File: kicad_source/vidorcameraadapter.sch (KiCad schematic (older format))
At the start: 9 parts, among them CN1 CONN_02X26, CN2 CONN_02X10, CN3 CONN_01X03

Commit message: corrected spacers, added resistors, made layout
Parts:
- added R1, R10, R11, R12, R13, R14, R15, R16, R17, R18, R2, R3, R4, R5, R6, R7, R8, R9: R_0603, resistors:R_0603, symbol devices:R_0603
- MECH1, MECH2: value WA-SMSI_9774010243 -> WA-SMSI_9774015151; footprint MECH_smd-spacer:WA-SMSI_9774010243 -> MECH_smd-spacer:WA-SMSI_9774015151; symbol MECH_smd-spacer:WA-SMSI_9774010243 -> MECH_smd-spacer:WA-SMSI_9774015151
- MECH3, MECH4, MECH5, MECH6: value WA-SMSI_9774010243 -> WA-SMSI_97730606334; footprint MECH_smd-spacer:WA-SMSI_9774010243 -> MECH_smd-spacer:WA-SMSI_97730606334; symbol MECH_smd-spacer:WA-SMSI_9774010243 -> MECH_smd-spacer:WA-SMSI_97730606334
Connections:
- net labels added: DOUT0_R, DOUT1_R, DOUT2_R, DOUT3_R, DOUT4_R, DOUT5_R, DOUT6_R, DOUT7_R, DOUT8_R, DOUT9_R, HREF_R, PCLK_R, PWDN_R, RST_R, SCL_R, SDA_R, VSYNC_R, XCLK_R
- wire segments 97 -> 115
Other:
- moved on the sheet: CN2

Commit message: added 3d models, added mounting holes
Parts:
- CN2: footprint pin_headers:Pin_Header_Straight_2x10 -> CON_wuerth:WR-PHD_61302021821
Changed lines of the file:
@@
 F 0 "CN2" H 7200 2665 50  0000 C CNN
 F 1 "CONN_02X10" H 7200 2574 50  0000 C CNN
-F 2 "pin_headers:Pin_Header_Straight_2x10" H 7200 2573 50  0001 C CNN
+F 2 "CON_wuerth:WR-PHD_61302021821" H 7200 2573 50  0001 C CNN
 F 3 "" H 7200 800 50  0000 C CNN
 	1    7200 2000

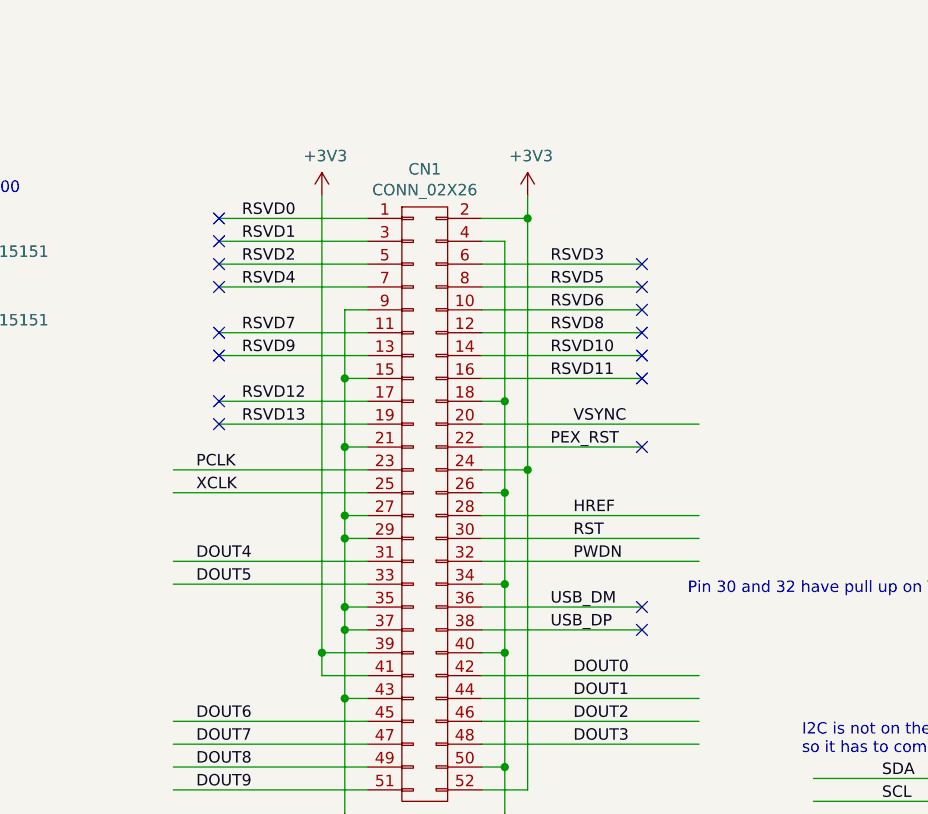
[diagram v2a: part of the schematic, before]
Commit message: added testpoints for all unused pins
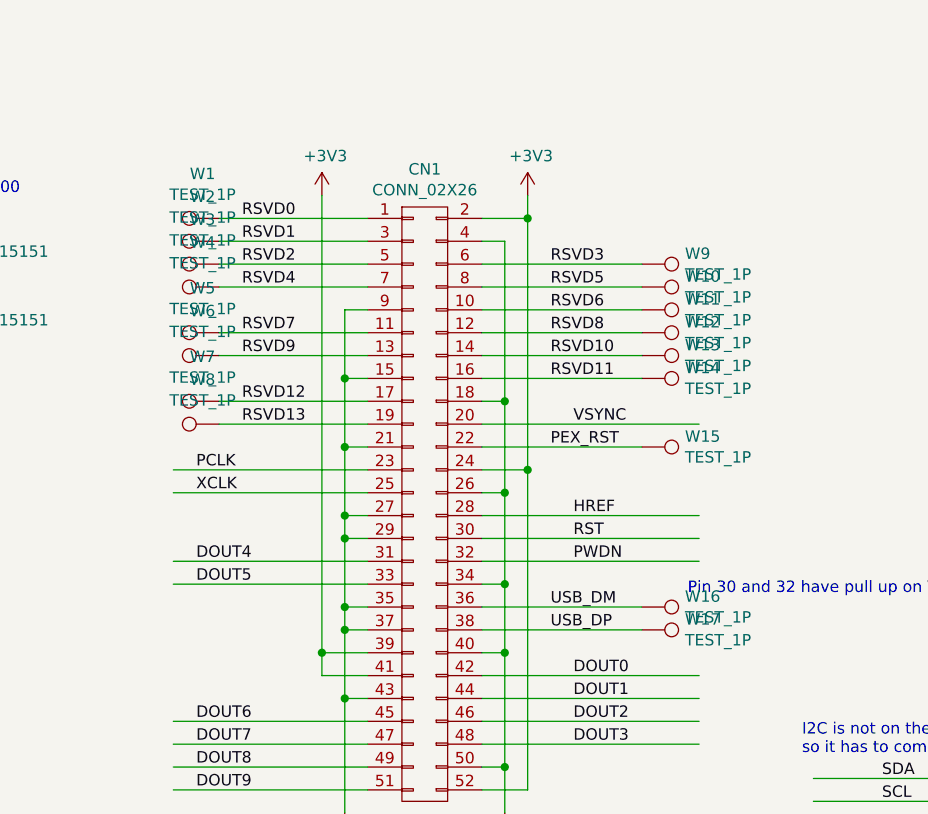
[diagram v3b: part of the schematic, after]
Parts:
- added W1, W10, W11, W12, W13, W14, W15, W16, W17, W2, W3, W4, W5, W6, W7, W8, W9: TEST_1P, wire_pads:SolderWirePad_single_1mmSMD, symbol mechanical-connectors:TEST_1P
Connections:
- no-connect marks 23 -> 6
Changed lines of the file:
@@
 Text Label 4100 6000 0    50   ~ 0
 USB_DP
-NoConn ~ 4500 5900
-NoConn ~ 4500 6000
 $Comp
 L mechanical-connectors:CONN_02X10 CN2
@@
 Text Notes 4700 5850 0    50   ~ 0
 Pin 30 and 32 have pull up on Vidor 4000
-NoConn ~ 4500 5200
 Wire Wire Line
 	2650 4200 3300 4200
@@
 Text Label 2750 5100 0    50   ~ 0
 RSVD13
-NoConn ~ 4500 4400
-NoConn ~ 4500 4500
-NoConn ~ 4500 4600
-NoConn ~ 4500 4700
-NoConn ~ 4500 4800
-NoConn ~ 4500 4900
-NoConn ~ 2650 4200
-NoConn ~ 2650 4300
-NoConn ~ 2650 4400
-NoConn ~ 2650 4500
-NoConn ~ 2650 4700
-NoConn ~ 2650 4800
-NoConn ~ 2650 5000
-NoConn ~ 2650 5100
 $Comp
 L MECH_smd-spacer:WA-SMSI_9774015151 MECH1
@@
 Text Label 7750 2050 0    50   ~ 0
 DOUT6_R
+$Comp
+L mechanical-connectors:TEST_1P W9
+U 1 1 5E310C83
+P 4500 4400
+F 0 "W9" V 4454 4588 50  0000 L CNN
+F 1 "TEST_1P" V 4545 4588 50  0000 L CNN
+F 2 "wire_pads:SolderWirePad_single_1mmSMD" V 4591 4588 50  0001 L CNN
+F 3 "" H 4700 4400 50  0000 C CNN
+	1    4500 4400
+	0    1    1    0
+$EndComp
+$Comp
+L mechanical-connectors:TEST_1P W10
+U 1 1 5E3153CE
+P 4500 4500
+F 0 "W10" V 4454 4688 50  0000 L CNN
+F 1 "TEST_1P" V 4545 4688 50  0000 L CNN
+F 2 "wire_pads:SolderWirePad_single_1mmSMD" V 4591 4688 50  0001 L CNN
+F 3 "" H 4700 4500 50  0000 C CNN
+	1    4500 4500
+	0    1    1    0
+$EndComp
+$Comp
+L mechanical-connectors:TEST_1P W11
+U 1 1 5E31571A
+P 4500 4600
+F 0 "W11" V 4454 4788 50  0000 L CNN
+F 1 "TEST_1P" V 4545 4788 50  0000 L CNN
+F 2 "wire_pads:SolderWirePad_single_1mmSMD" V 4591 4788 50  0001 L CNN
+F 3 "" H 4700 4600 50  0000 C CNN
+	1    4500 4600
+	0    1    1    0
+$EndComp
+$Comp
+L mechanical-connectors:TEST_1P W12
+U 1 1 5E3158F5
+P 4500 4700
+F 0 "W12" V 4454 4888 50  0000 L CNN
+F 1 "TEST_1P" V 4545 4888 50  0000 L CNN
+F 2 "wire_pads:SolderWirePad_single_1mmSMD" V 4591 4888 50  0001 L CNN
+F 3 "" H 4700 4700 50  0000 C CNN
+	1    4500 4700
+	0    1    1    0
+$EndComp
+$Comp
+L mechanical-connectors:TEST_1P W13
+U 1 1 5E315B8E
+P 4500 4800
+F 0 "W13" V 4454 4988 50  0000 L CNN
+F 1 "TEST_1P" V 4545 4988 50  0000 L CNN
+F 2 "wire_pads:SolderWirePad_single_1mmSMD" V 4591 4988 50  0001 L CNN
+F 3 "" H 4700 4800 50  0000 C CNN
+	1    4500 4800
+	0    1    1    0
+$EndComp
+$Comp
+L mechanical-connectors:TEST_1P W14
+U 1 1 5E315D78
+P 4500 4900
+F 0 "W14" V 4454 5088 50  0000 L CNN
+F 1 "TEST_1P" V 4545 5088 50  0000 L CNN
+F 2 "wire_pads:SolderWirePad_single_1mmSMD" V 4591 5088 50  0001 L CNN
+F 3 "" H 4700 4900 50  0000 C CNN
+	1    4500 4900
+	0    1    1    0
+$EndComp
+$Comp
+L mechanical-connectors:TEST_1P W15
+U 1 1 5E315FB3
+P 4500 5200
+F 0 "W15" V 4454 5388 50  0000 L CNN
+F 1 "TEST_1P" V 4545 5388 50  0000 L CNN
+F 2 "wire_pads:SolderWirePad_single_1mmSMD" V 4591 5388 50  0001 L CNN
+F 3 "" H 4700 5200 50  0000 C CNN
+	1    4500 5200
+	0    1    1    0
+$EndComp
+$Comp
+L mechanical-connectors:TEST_1P W16
+U 1 1 5E316676
+P 4500 5900
+F 0 "W16" V 4454 6088 50  0000 L CNN
+F 1 "TEST_1P" V 4545 6088 50  0000 L CNN
+F 2 "wire_pads:SolderWirePad_single_1mmSMD" V 4591 6088 50  0001 L CNN
+F 3 "" H 4700 5900 50  0000 C CNN
+	1    4500 5900
+	0    1    1    0
+$EndComp
+$Comp
+L mechanical-connectors:TEST_1P W17
+U 1 1 5E316F5D
+P 4500 6000
+F 0 "W17" V 4454 6188 50  0000 L CNN
+F 1 "TEST_1P" V 4545 6188 50  0000 L CNN
+F 2 "wire_pads:SolderWirePad_single_1mmSMD" V 4591 6188 50  0001 L CNN
+F 3 "" H 4700 6000 50  0000 C CNN
+	1    4500 6000
+	0    1    1    0
+$EndComp
+$Comp
+L mechanical-connectors:TEST_1P W8
+U 1 1 5E317186
+P 2650 5100
+F 0 "W8" V 2845 5172 50  0000 C CNN
+F 1 "TEST_1P" V 2754 5172 50  0000 C CNN
+F 2 "wire_pads:SolderWirePad_single_1mmSMD" V 2741 5288 50  0001 L CNN
+F 3 "" H 2850 5100 50  0000 C CNN
+	1    2650 5100
+	0    -1   -1   0
+$EndComp
+$Comp
+L mechanical-connectors:TEST_1P W7
+U 1 1 5E31844B
+P 2650 5000
+F 0 "W7" V 2845 5072 50  0000 C CNN
+F 1 "TEST_1P" V 2754 5072 50  0000 C CNN
+F 2 "wire_pads:SolderWirePad_single_1mmSMD" V 2741 5188 50  0001 L CNN
+F 3 "" H 2850 5000 50  0000 C CNN
+	1    2650 5000
+	0    -1   -1   0
+$EndComp
+$Comp
+L mechanical-connectors:TEST_1P W6
+U 1 1 5E318681
+P 2650 4800
+F 0 "W6" V 2845 4872 50  0000 C CNN
+F 1 "TEST_1P" V 2754 4872 50  0000 C CNN
+F 2 "wire_pads:SolderWirePad_single_1mmSMD" V 2741 4988 50  0001 L CNN
+F 3 "" H 2850 4800 50  0000 C CNN
+	1    2650 4800
+	0    -1   -1   0
+$EndComp
+$Comp
+L mechanical-connectors:TEST_1P W5
+U 1 1 5E31885D
+P 2650 4700
+F 0 "W5" V 2845 4772 50  0000 C CNN
+F 1 "TEST_1P" V 2754 4772 50  0000 C CNN
+F 2 "wire_pads:SolderWirePad_single_1mmSMD" V 2741 4888 50  0001 L CNN
+F 3 "" H 2850 4700 50  0000 C CNN
+	1    2650 4700
+	0    -1   -1   0
+$EndComp
+$Comp
+L mechanical-connectors:TEST_1P W4
+U 1 1 5E3198A2
+P 2650 4500
+F 0 "W4" V 2845 4572 50  0000 C CNN
+F 1 "TEST_1P" V 2754 4572 50  0000 C CNN
+F 2 "wire_pads:SolderWirePad_single_1mmSMD" V 2741 4688 50  0001 L CNN
+F 3 "" H 2850 4500 50  0000 C CNN
+	1    2650 4500
+	0    -1   -1   0
+$EndComp
+$Comp
+L mechanical-connectors:TEST_1P W3
+U 1 1 5E319C0A
+P 2650 4400
+F 0 "W3" V 2845 4472 50  0000 C CNN
+F 1 "TEST_1P" V 2754 4472 50  0000 C CNN
+F 2 "wire_pads:SolderWirePad_single_1mmSMD" V 2741 4588 50  0001 L CNN
+F 3 "" H 2850 4400 50  0000 C CNN
+	1    2650 4400
+	0    -1   -1   0
+$EndComp
+$Comp
+L mechanical-connectors:TEST_1P W2
+U 1 1 5E319E50
+P 2650 4300
+F 0 "W2" V 2845 4372 50  0000 C CNN
+F 1 "TEST_1P" V 2754 4372 50  0000 C CNN
+F 2 "wire_pads:SolderWirePad_single_1mmSMD" V 2741 4488 50  0001 L CNN
+F 3 "" H 2850 4300 50  0000 C CNN
+	1    2650 4300
+	0    -1   -1   0
+$EndComp
+$Comp
+L mechanical-connectors:TEST_1P W1
+U 1 1 5E31A08D
+P 2650 4200
+F 0 "W1" V 2845 4272 50  0000 C CNN
+F 1 "TEST_1P" V 2754 4272 50  0000 C CNN
+F 2 "wire_pads:SolderWirePad_single_1mmSMD" V 2741 4388 50  0001 L CNN
+F 3 "" H 2850 4200 50  0000 C CNN
+	1    2650 4200
+	0    -1   -1   0
+$EndComp
 $EndSCHEMATC

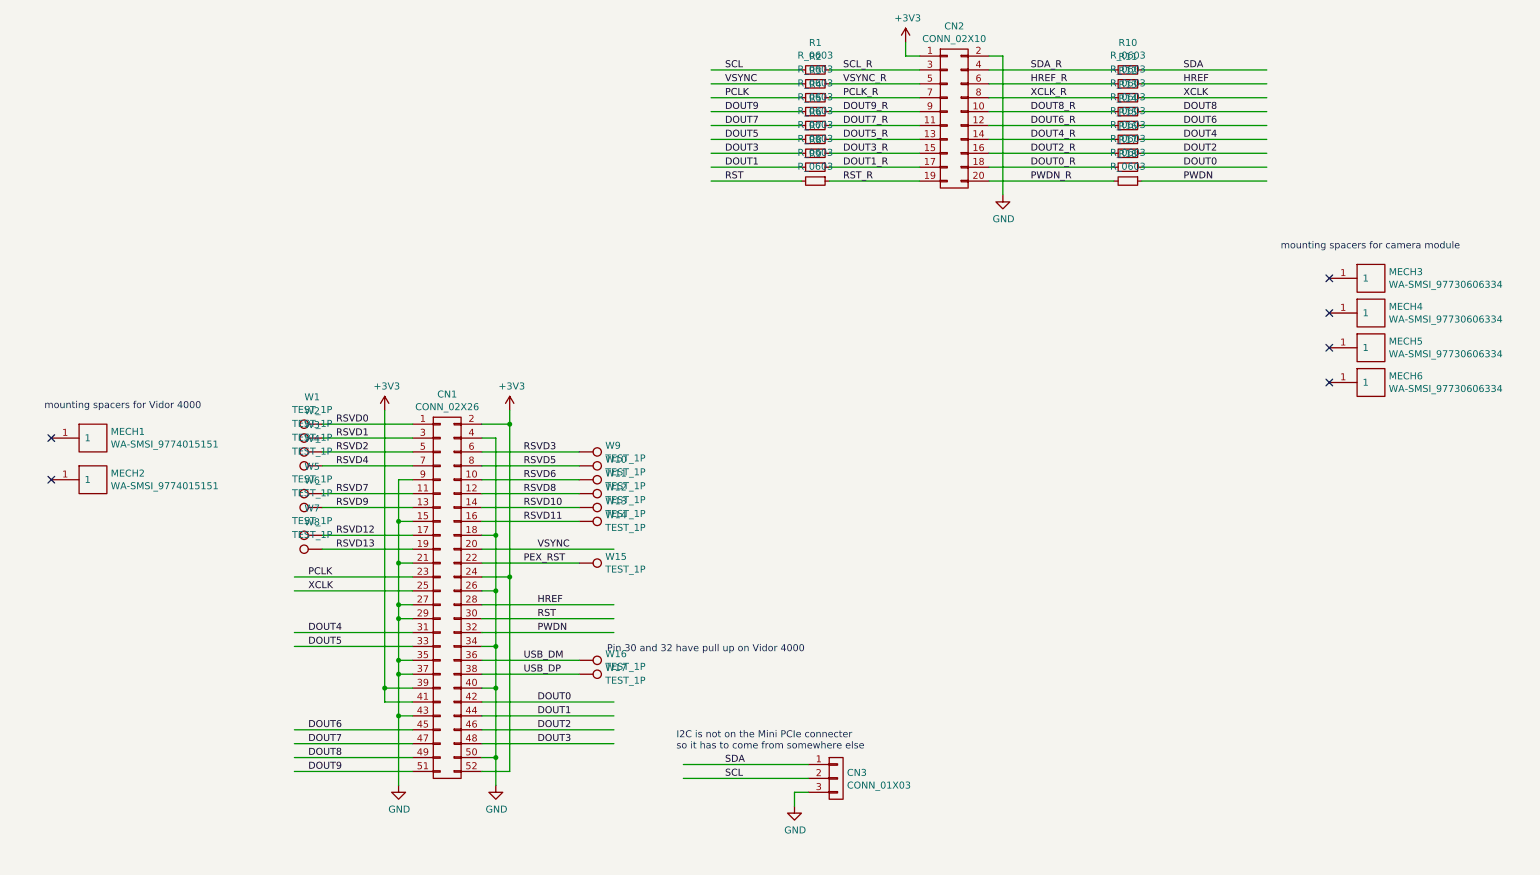
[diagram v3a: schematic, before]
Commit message: updated layout, made edge smoother, generated pdf schematic and images
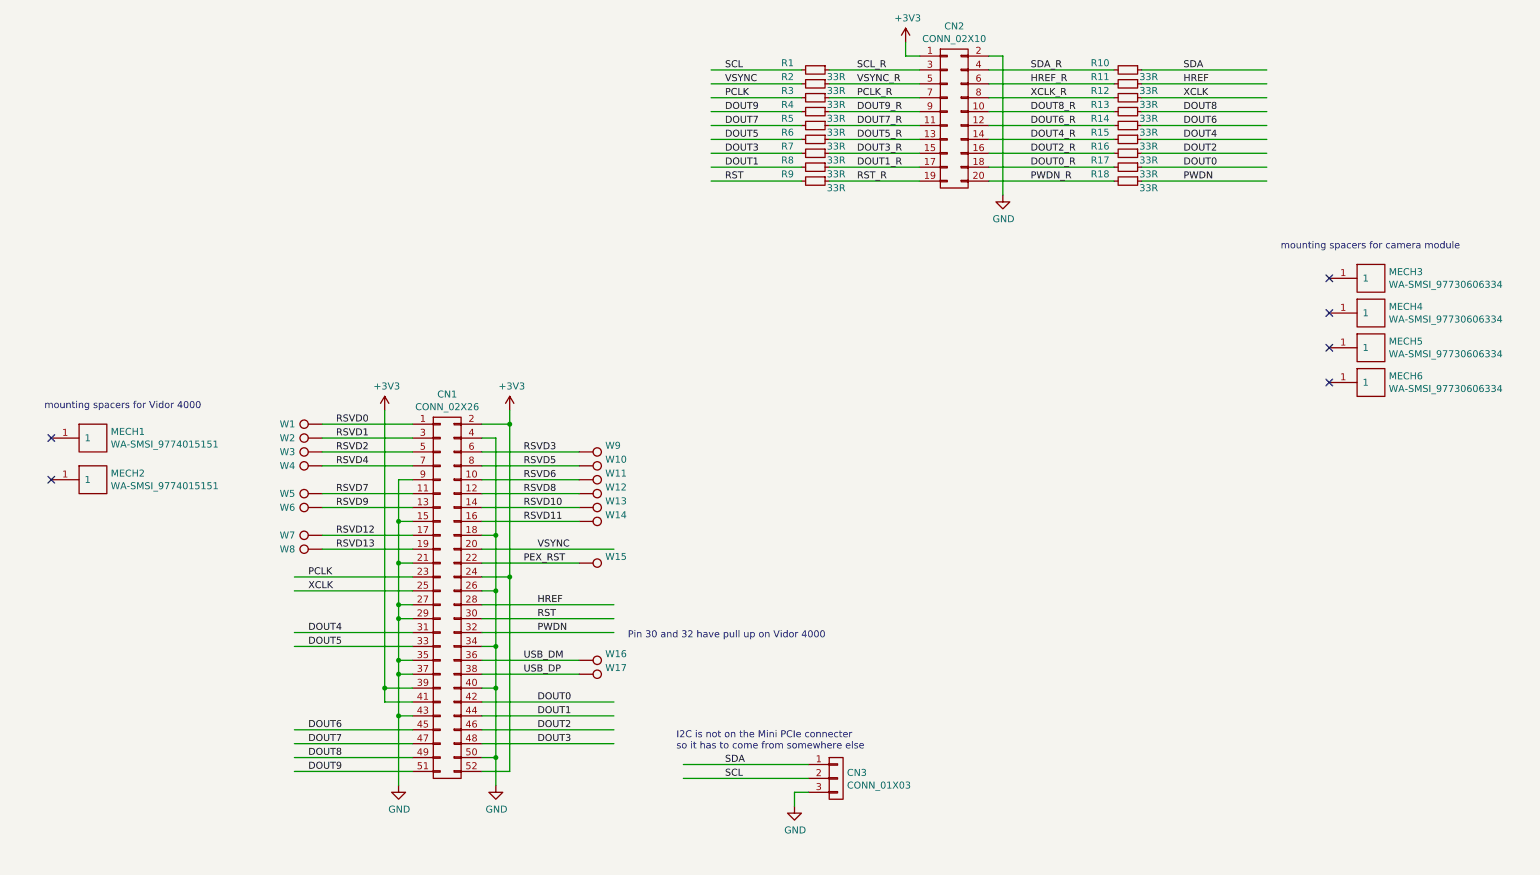
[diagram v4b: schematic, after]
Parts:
- R1, R10, R11, R12, R13, R14, R15, R16, R17, R18, R2, R3, R4, R5, R6, R7, R8, R9: value R_0603 -> 33R
